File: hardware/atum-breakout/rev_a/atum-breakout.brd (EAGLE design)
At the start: 63.5 x 63.5 mm, 71 parts, among them J1 TC2030-CTX, J2 TC2030-CC2538-BL, J3 SCREW-TERMINAL_8_0.100, J4 SCREW-TERMINAL_7_0.100, J5 SCREW-TERMINAL_7_0.100, J6 SCREW-TERMINAL_8_0.100, J7 MICRO_USB_B_HIROSE_ZX62R-B-5P, J8 SCREW-TERMINAL_3_0.100, J9 SCREW-TERMINAL_3_0.100, U1 ATUM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

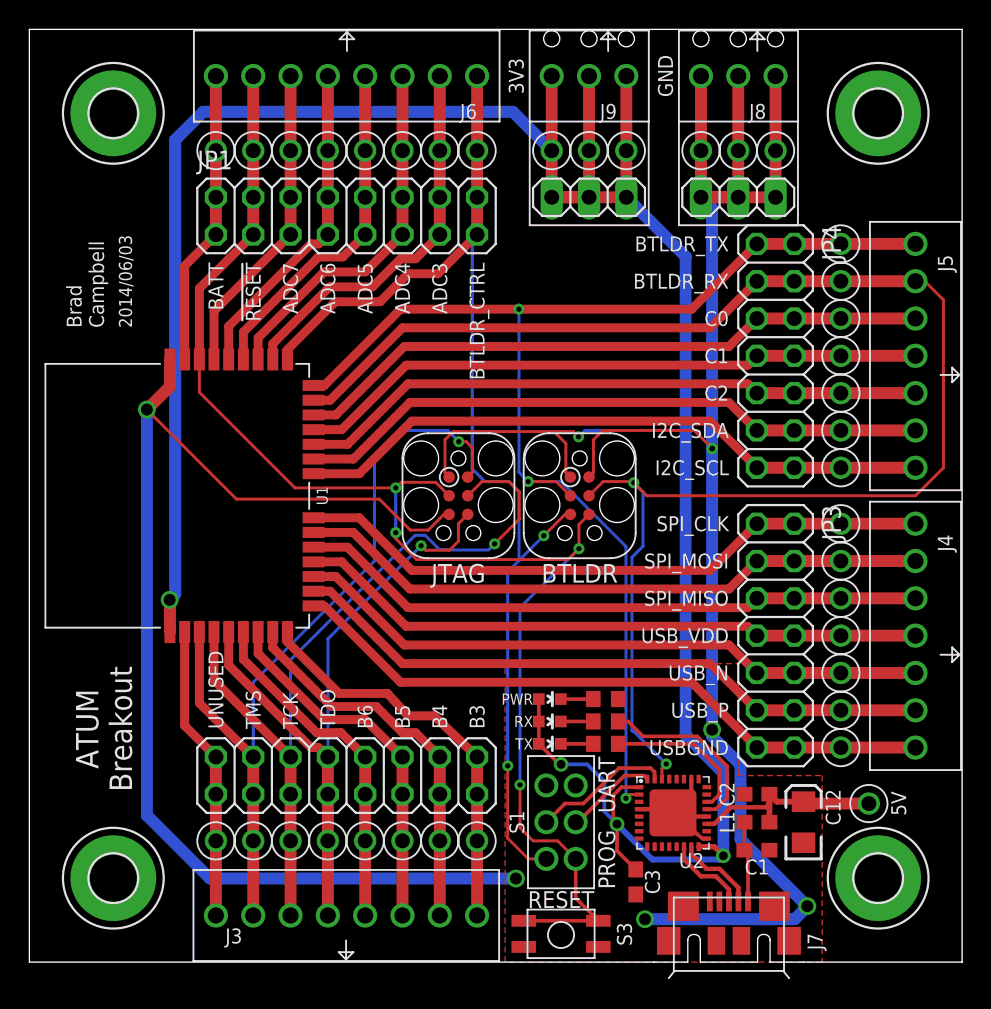
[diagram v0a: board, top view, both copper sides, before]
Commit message: updated part labels
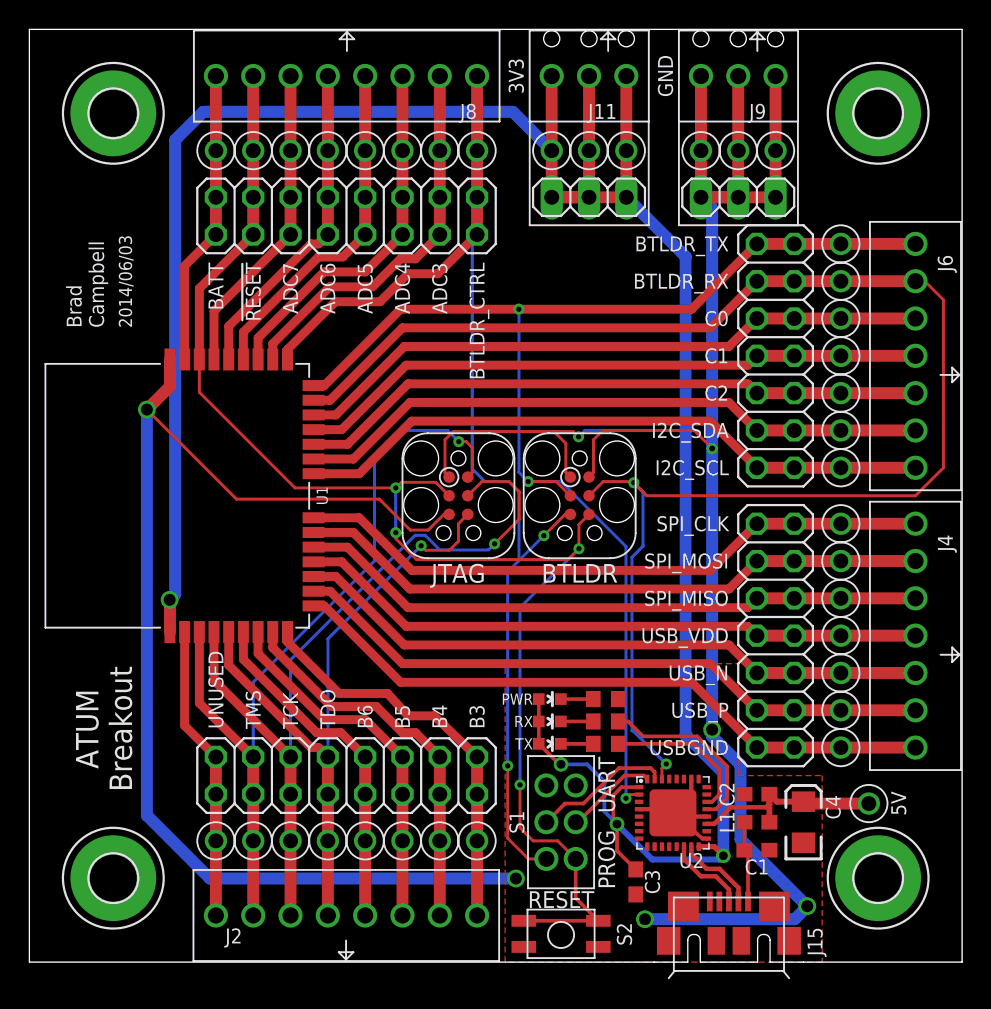
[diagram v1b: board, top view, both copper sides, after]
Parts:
- removed JP1, JP2: (no value), pinhead:2X08
- removed JP3, JP4: (no value), pinhead:2X07
- added J11: SCREW-TERMINAL_3_0.100, headers:CONN_BLOCK_3
- added J13: TC2030-CTX, connector:TC2030-IDC
- added J14: TC2030-CC2538-BL, connector:TC2030-IDC
- added J15: MICRO_USB_B_HIROSE_ZX62R-B-5P, connector:USB_MICRO_B-HIROSE-ZX62R-B-5P
- J1: value TC2030-CTX -> (none); device connector:TC2030-IDC -> pinhead:2X08
- J2: value TC2030-CC2538-BL -> SCREW-TERMINAL_8_0.100; device connector:TC2030-IDC -> headers:CONN_BLOCK_8
- J3: value SCREW-TERMINAL_8_0.100 -> (none); device headers:CONN_BLOCK_8 -> pinhead:2X07
- J5: value SCREW-TERMINAL_7_0.100 -> (none); device headers:CONN_BLOCK_7 -> pinhead:2X07
- J6: value SCREW-TERMINAL_8_0.100 -> SCREW-TERMINAL_7_0.100; device headers:CONN_BLOCK_8 -> headers:CONN_BLOCK_7
- J7: value MICRO_USB_B_HIROSE_ZX62R-B-5P -> (none); device connector:USB_MICRO_B-HIROSE-ZX62R-B-5P -> pinhead:2X08
- J8: value SCREW-TERMINAL_3_0.100 -> SCREW-TERMINAL_8_0.100; device headers:CONN_BLOCK_3 -> headers:CONN_BLOCK_8
- moved J7 57.1 mm to (21.6, 50.8)
- moved J6 43.2 mm to (60.3, 41.3), turned to 90 degrees
- moved J3 34.9 mm to (50.8, 22.2), turned to 270 degrees
- moved J2 32.7 mm to (21.6, 3.17), turned to 0 degrees
- moved J8 26.7 mm to (21.6, 60.3)
- moved J1 20.5 mm to (21.6, 12.7), turned to 0 degrees
- moved J9 10.2 mm to (48.3, 60.3)
- moved J5 9.53 mm to (50.8, 41.3), turned to 270 degrees
- renumbered C12 to C4, JP5 to J10, JP6 to J12, S3 to S2
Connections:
- net !RESET: now also J13.3, J14.6, J7.3, J7.4, J8.7; no longer J1.3, J2.6, J6.7, JP1.3, JP1.4
- net ADC3: now also J7.13, J7.14, J8.2; no longer J6.2, JP1.13, JP1.14
- net ADC4: now also J7.11, J7.12, J8.3; no longer J6.3, JP1.11, JP1.12
- net ADC5: now also J7.10, J7.9, J8.4; no longer J6.4, JP1.10, JP1.9
- net ADC6: now also J7.7, J7.8, J8.5; no longer J6.5, JP1.7, JP1.8
- net ADC7: now also J7.5, J7.6, J8.6; no longer J6.6, JP1.5, JP1.6
- net B3: now also J1.15, J1.16, J2.8; no longer J3.8, JP2.15, JP2.16
- net B4: now also J1.13, J1.14, J2.7; no longer J3.7, JP2.13, JP2.14
- net B5: now also J1.11, J1.12, J2.6; no longer J3.6, JP2.11, JP2.12
- net B6: now also J1.10, J1.9, J2.5; no longer J3.5, JP2.10, JP2.9
- net BATTERY: now also J7.1, J7.2, J8.8; no longer J6.8, JP1.1, JP1.2
- net BOOTLOADER_CTRL: now also J14.5, J7.15, J7.16, J8.1; no longer J2.5, J6.1, JP1.15, JP1.16
- net BOOTLOADER_RX: now also J14.4, J5.3, J5.4, J6.6; no longer J2.4, J5.6, JP4.3, JP4.4
- net BOOTLOADER_TX: now also J14.3, J5.1, J5.2, J6.7; no longer J2.3, J5.7, JP4.1, JP4.2
- net C0: now also J5.6, J6.5; no longer JP4.5, JP4.6
- net C1: now also J5.7, J5.8, J6.4; no longer J5.4, JP4.7, JP4.8
- net C2: now also J5.10, J5.9, J6.3; no longer J5.3, JP4.10, JP4.9
- net DGND_USB: now also J3.13, J3.14; no longer JP3.13, JP3.14
- net DVDD_USB: now also J3.7, J3.8; no longer JP3.7, JP3.8
- net GND: now also J13.5, J14.2, J15.5, J9.1, J9.2, J9.3; no longer J1.5, J2.2, J7.5, J8.1, J8.2, J8.3
- net I2C_SCL: now also J5.13, J5.14, J6.1; no longer J5.1, JP4.13, JP4.14
- net I2C_SDA: now also J5.11, J5.12, J6.2; no longer J5.2, JP4.11, JP4.12
- net N$3: now also J15.2; no longer J7.2
- net N$4: now also J15.3; no longer J7.3
- net SPI_MISO: now also J3.5, J3.6; no longer JP3.5, JP3.6
- net SPI_MOSI: now also J3.3, J3.4; no longer JP3.3, JP3.4
- net SPI_SCK: now also J3.1, J3.2; no longer JP3.1, JP3.2
- net TCK: now also J1.5, J1.6, J13.4, J2.3; no longer J1.4, J3.3, JP2.5, JP2.6
- net TDO: now also J1.7, J1.8, J13.6, J2.4; no longer J1.6, J3.4, JP2.7, JP2.8
- net TMS: now also J1.3, J1.4, J13.2, J2.2; no longer J1.2, J3.2, JP2.3, JP2.4
- net UNUSED: now also J1.1, J1.2, J2.1; no longer J3.1, JP2.1, JP2.2
- net USB5V: now also J15.1; no longer J7.1
- net USB_N: now also J3.10, J3.9; no longer JP3.10, JP3.9
- net USB_P: now also J3.11, J3.12; no longer JP3.11, JP3.12
- net VCC: now also J11.1, J11.2, J11.3, J13.1, J14.1; no longer J1.1, J2.1, J9.1, J9.2, J9.3
